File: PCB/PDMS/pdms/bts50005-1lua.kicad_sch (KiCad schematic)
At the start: 13 parts, among them Q3 BTS500101LUAAUMA1

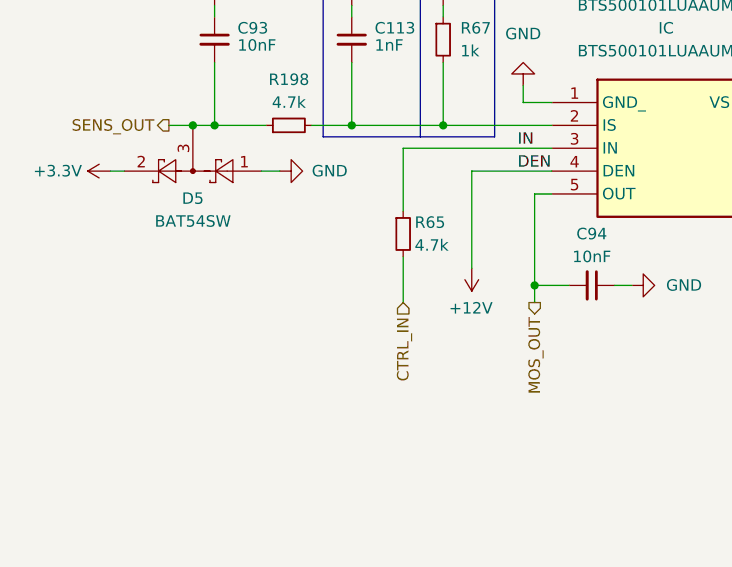
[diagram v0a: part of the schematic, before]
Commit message: Added can-bus software switching and major changes in layout
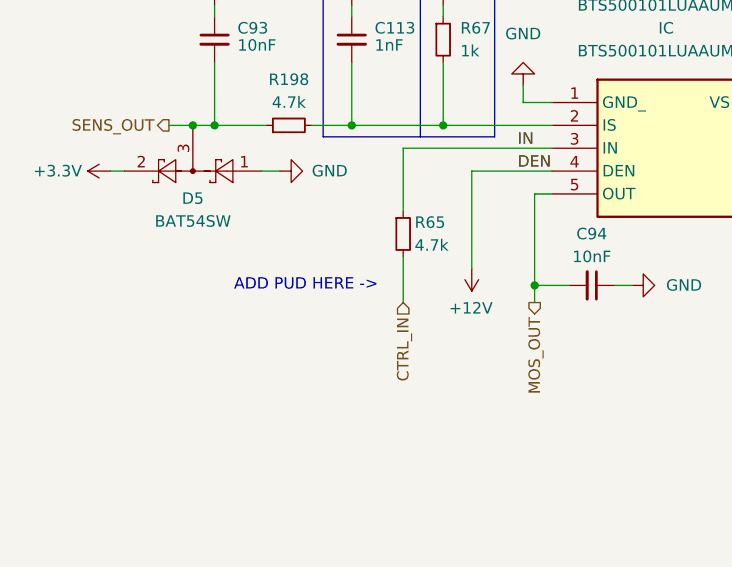
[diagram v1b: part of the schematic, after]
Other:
- note added: "ADD PUD HERE ->"
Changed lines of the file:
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@@
     (effects (font (size 0.6 0.6)) (justify left bottom))
+  )
+  (text "ADD PUD HERE ->" (at 39.624 83.312 0)
+    (effects (font (size 1.27 1.27)) (justify left bottom))
   )
   (text "BTS50010/05-1LUA Switch " (at 100.33 128.27 0)

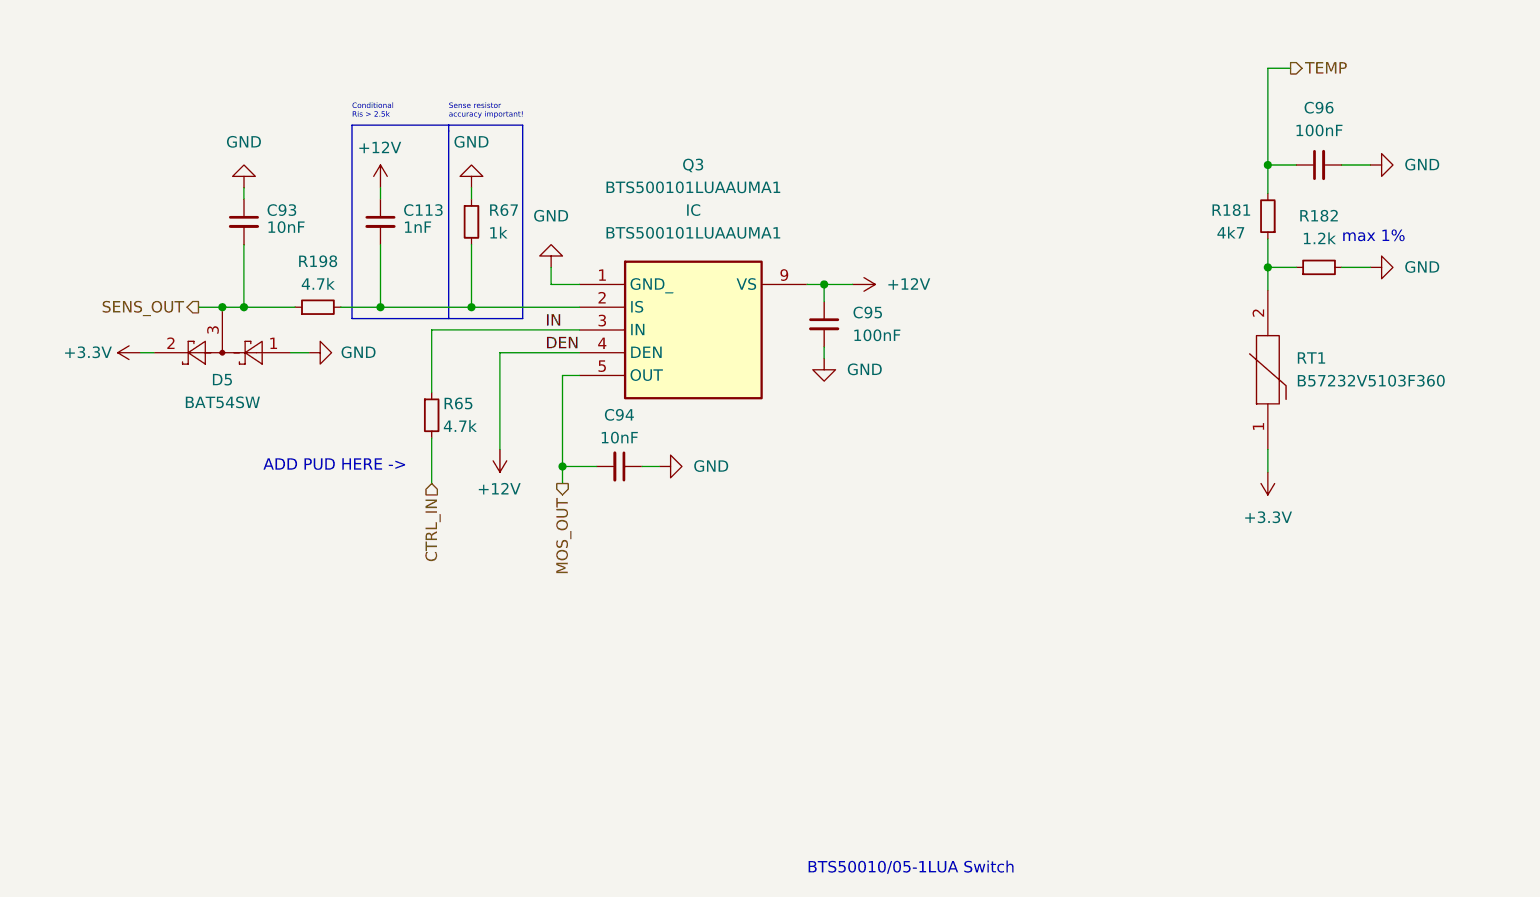
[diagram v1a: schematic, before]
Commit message: Finished layout - w/o stiching
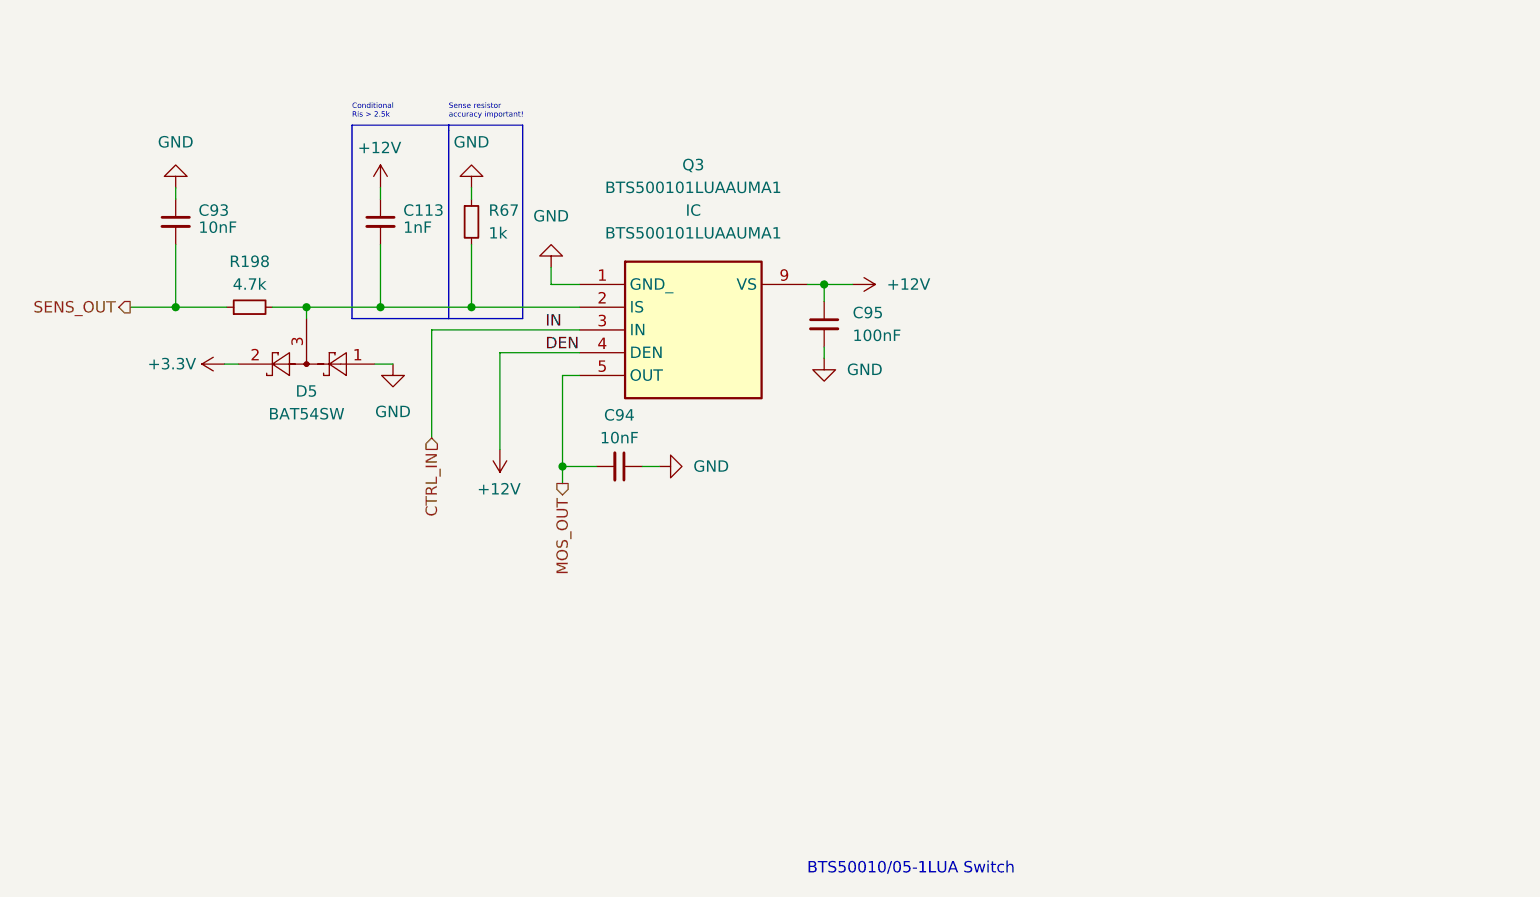
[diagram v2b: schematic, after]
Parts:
- removed C96: 100nF, Capacitor_SMD:C_0402_1005Metric, symbol Device:C_Small
- removed R181: 4k7, Resistor_SMD:R_0402_1005Metric, symbol Device:R_Small
- removed R182: 1.2k, Resistor_SMD:R_0402_1005Metric, symbol Device:R_Small
- removed R65: 4.7k, Resistor_SMD:R_0402_1005Metric, symbol Device:R_Small
- removed RT1: B57232V5103F360, PDM_Additional:THRMC1005X60N, symbol PDM_additional:B57232V5103F360
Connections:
- net IN is gone; now on net CTRL_IN: Q3.3 (IN)
- net SENS_OUT: no longer D5.3
- net at C113.2, Q3.2 (IS), R198.2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: now also D5.3
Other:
- note removed: "ADD PUD HERE ->"
- note removed: "max 1%"
- moved on the sheet: C93, D5, R198

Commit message: Finished 2024 version + gerbers
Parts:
- added D44: 3V3, Diode_SMD:D_SOD-523, symbol Device:D_Zener_Small
- added R9: 4.7k, Resistor_SMD:R_0402_1005Metric, symbol Device:R_Small
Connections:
- net GND: now also D44.2 (A)
- net at C113.2, Q3.2 (IS), R67.2: now also R9.2; no longer D5.3, R198.2
- new net: D44.1 (K), D5.3, R198.2, R9.1
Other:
- note added: "Check if RC filter values are correct: Sense signal filtering A time constant (RADC * CSENSE ) longer than 1 μs is recommended"
- note added: "Ris_prot -> value should be checked properly"
- note added: "SZMM5Z3V3T1G"
- moved on the sheet: C113, C93, C94, C95, D5, Q3, R198, R67

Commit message: Clean-up of schematics
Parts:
- renumbered R9 to R107
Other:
- note added: "BTS50010/05-1LUA High side switch"
- note removed: "BTS50010/05-1LUA Switch"
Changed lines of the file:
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@@
     (effects (font (size 0.6 0.6)) (justify left bottom))
   )
-  (text "BTS50010/05-1LUA Switch " (at 100.33 128.27 0)
+  (text "BTS50010/05-1LUA High side switch " (at 100.33 128.27 0)
     (effects (font (size 1.27 1.27)) (justify left bottom))
   )
@@
   (symbol (lib_id "BTS500101LUAAUMA1:BTS500101LUAAUMA1") (at 110.363 62.738 0) (unit 1)
     (in_bom yes) (on_board yes) (fields_autoplaced)
-    (property "Reference" "Q3" (id 0) (at 123.063 49.403 0))
-    (property "Value" "BTS500101LUAAUMA1" (id 1) (at 123.063 51.943 0))
+    (property "Reference" "Q3" (id 0) (at 123.063 54.61 0))
+    (property "Value" "BTS500101LUAAUMA1" (id 1) (at 123.063 57.15 0))
     (property "Footprint" "PDM_Additional:BTS500101LUAAUMA1" (id 2) (at 110.363 62.738 0)
       (effects (font (size 1.27 1.27)) hide)
@@
       (effects (font (size 1.27 1.27)) hide)
     )
-    (property "Reference_1" "IC" (id 4) (at 123.063 54.483 0))
-    (property "Value_1" "BTS500101LUAAUMA1" (id 5) (at 123.063 57.023 0))
+    (property "Reference_1" "IC" (id 4) (at 123.063 54.483 0)
+      (effects (font (size 1.27 1.27)) hide)
+    )
+    (property "Value_1" "BTS500101LUAAUMA1" (id 5) (at 123.063 57.15 0)
+      (effects (font (size 1.27 1.27)) hide)
+    )
     (property "Footprint_1" "BTS500101LUAAUMA1" (id 6) (at 131.953 157.658 0)
       (effects (font (size 1.27 1.27)) (justify left top) hide)
@@
   (symbol (lib_id "Device:R_Small") (at 80.01 65.278 90) (unit 1)
     (in_bom yes) (on_board yes)
-    (property "Reference" "R9" (id 0) (at 80.01 60.198 90))
+    (property "Reference" "R107" (id 0) (at 80.01 60.198 90))
     (property "Value" "4.7k" (id 1) (at 80.01 62.738 90))
     (property "Footprint" "Resistor_SMD:R_0402_1005Metric" (id 2) (at 80.01 65.278 0)
@@
   (symbol (lib_id "power:GND") (at 66.421 51.943 180) (unit 1)
     (in_bom yes) (on_board yes)
-    (property "Reference" "#PWR0148" (id 0) (at 66.421 45.593 0)
-      (effects (font (size 1.27 1.27)) hide)
-    )
+    (property "Reference" "#PWR0151" (id 0) (at 66.421 45.593 0)
+      (effects (font (size 1.27 1.27)) hide)
+    )

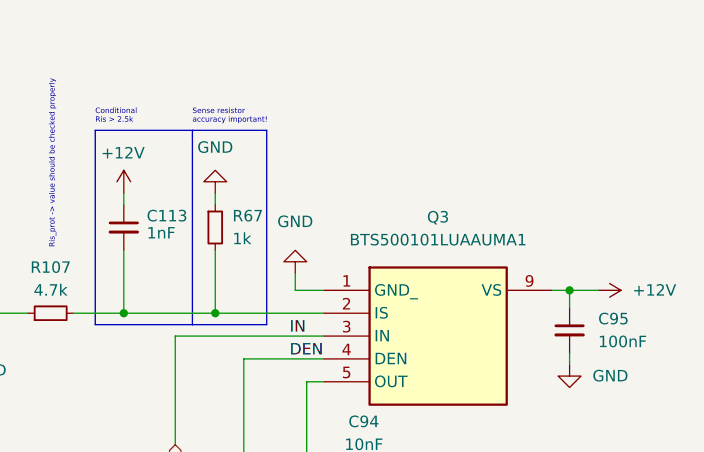
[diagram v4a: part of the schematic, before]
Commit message: Changes after board 4.1 first unit assembly
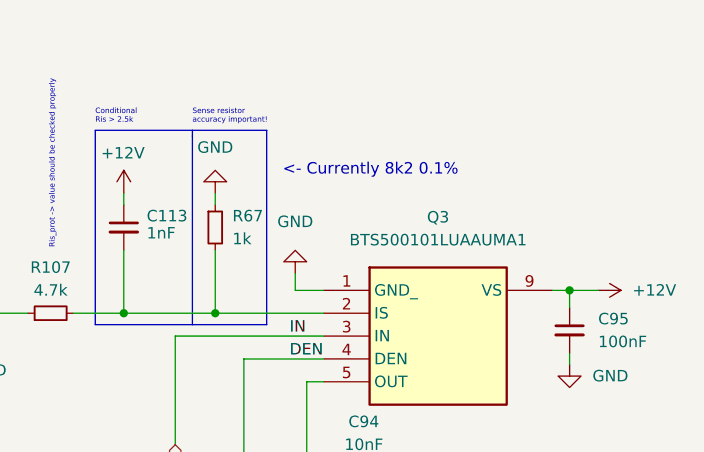
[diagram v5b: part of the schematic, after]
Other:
- note added: "<- Currently 8k2 0.1%"
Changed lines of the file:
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@@
     (effects (font (size 0.6 0.6)) (justify left bottom))
+  )
+  (text "<- Currently 8k2 0.1%" (at 105.791 50.165 0)
+    (effects (font (size 1.27 1.27)) (justify left bottom))
   )
   (text "Ris_prot -> value should be checked properly" (at 80.518 58.166 90)

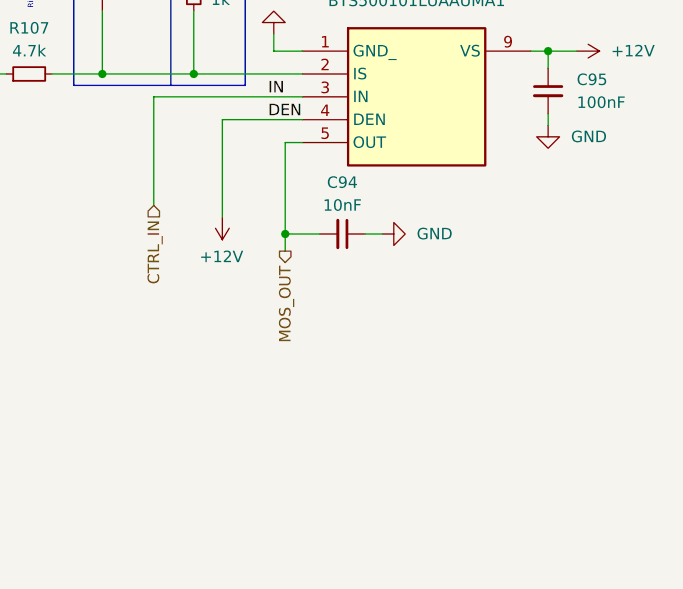
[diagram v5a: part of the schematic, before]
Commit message: Added fuses to main output channels
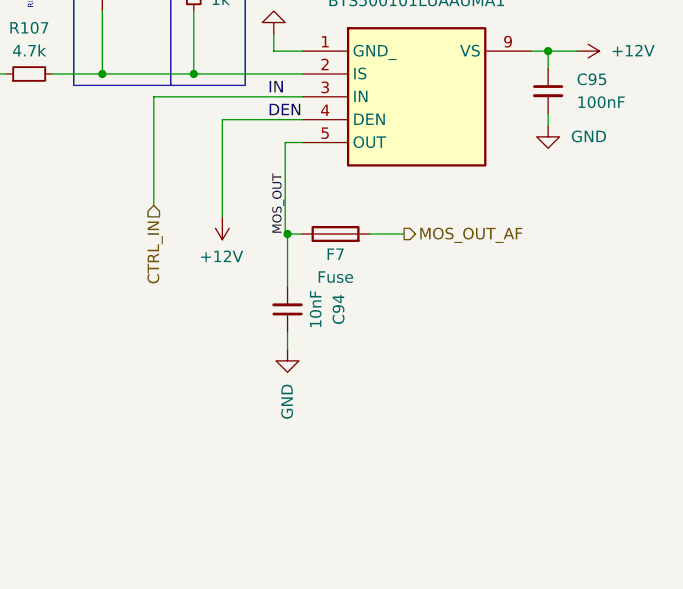
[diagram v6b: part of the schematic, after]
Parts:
- added F7: Fuse, Fuse:Fuse_1206_3216Metric, symbol Device:Fuse
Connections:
- net MOS_OUT: now also F7.1
- new net MOS_OUT_AF: F7.2
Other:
- moved on the sheet: C94
